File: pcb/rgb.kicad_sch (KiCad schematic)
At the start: 29 parts, among them J1 2.54-2*8P, J3 B4PS-VH, J4 TYPE-C-31-M-12, J5 TF-01A, J7 B4PS-VH, U4 EVQQ2, U5 ESP32-WROOM-32E, U7 CH340C, U8 SPX3819M5-L, U9 CH224K

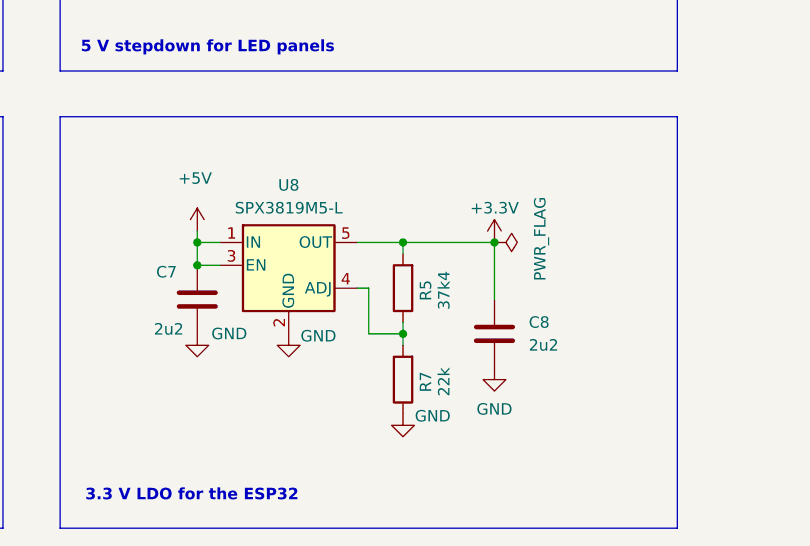
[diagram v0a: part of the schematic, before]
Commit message: pcb: increase esp32 voltage slightly
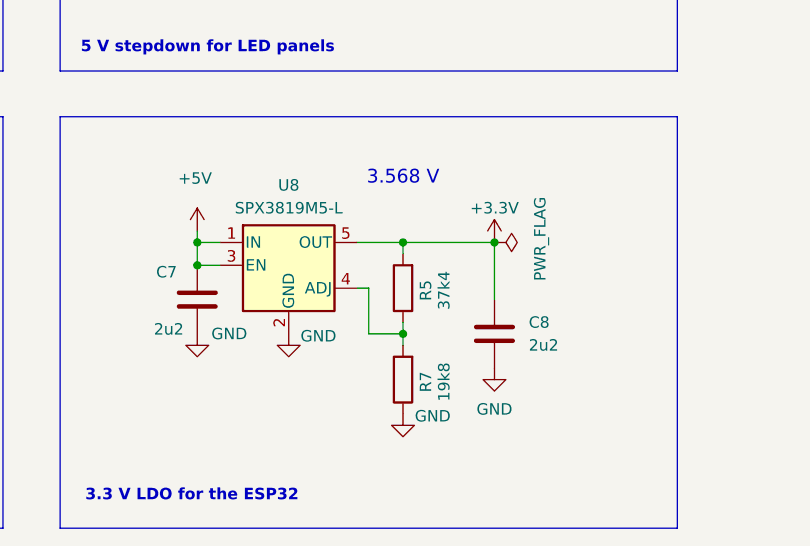
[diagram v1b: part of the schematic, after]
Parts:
- R7: value 22k -> 19k8
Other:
- note added: "3.568 V"
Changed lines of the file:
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@@
+		)
+	)
+	(text "3.568 V"
+		(exclude_from_sim no)
+		(at 133.35 144.018 0)
+		(effects
+			(font
+				(size 1.524 1.524)
+			)
 		)
 	)
@@
 			)
 		)
-		(property "Value" "22k"
+		(property "Value" "19k8"
 			(at 137.922 166.624 90)
 			(effects

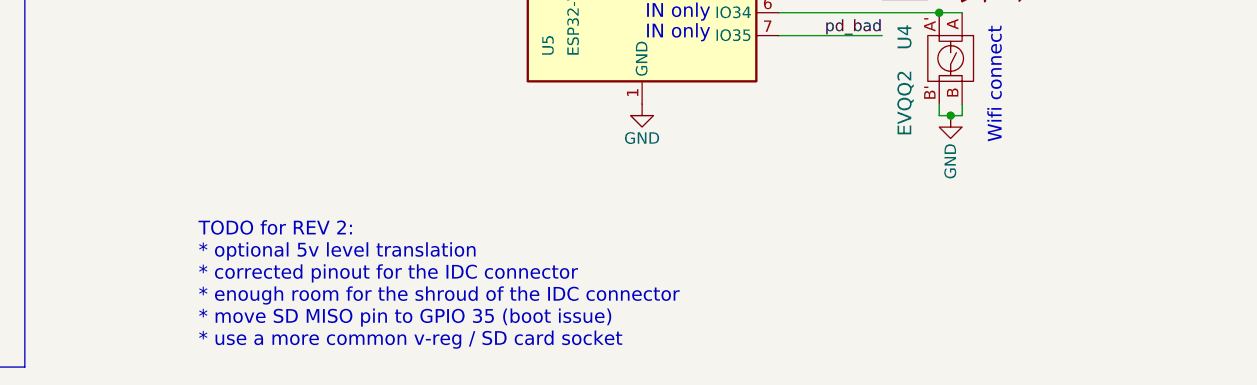
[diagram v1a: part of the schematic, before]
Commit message: hardware bug, swap IO 12 and 33
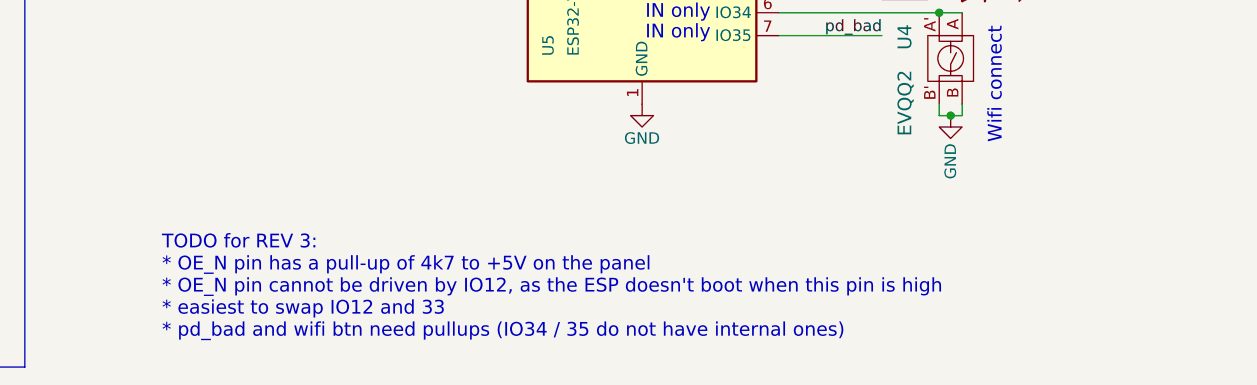
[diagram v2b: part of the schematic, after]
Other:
- note added: "TODO for REV 3: * OE_N pin has a pull-up of 4k7 to +5V on the panel * OE_N pin cannot be driven by IO12, as the ESP doesn't boot when this pin is high * easiest to swap IO12 and 33 * pd_bad and wifi btn need pullups (IO34 / 35 do not have internal ones)"
- note removed: "TODO for REV 2: * optional 5v level translation * corrected pinout for the IDC connector * enough room for the shroud of the IDC connector * move SD MISO pin to GPIO 35 (boot issue) * use a more common v-reg / SD card socket"
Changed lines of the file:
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@@
 		)
 	)
-	(text "TODO for REV 2:\n* optional 5v level translation\n* corrected pinout for the IDC connector\n* enough room for the shroud of the IDC connector\n* move SD MISO pin to GPIO 35 (boot issue)\n* use a more common v-reg / SD card socket"
+	(text "TODO for REV 3:\n* OE_N pin has a pull-up of 4k7 to +5V on the panel\n* OE_N pin cannot be driven by IO12, as the ESP doesn't boot when this pin is high\n* easiest to swap IO12 and 33\n* pd_bad and wifi btn need pullups (IO34 / 35 do not have internal ones)\n"
 		(exclude_from_sim no)
-		(at 183.134 180.848 0)
+		(at 179.07 179.832 0)
 		(effects
 			(font

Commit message: schematic: one more item for the todo list
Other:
- note added: "* Connect SD card to the fixed pins of the MMC-interface. Because the SD-SPI driver in IDF-V5 does seek very slowly"
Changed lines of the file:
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@@
+		)
+	)
+	(text "*  Connect SD card to the fixed pins of the MMC-interface.\n   Because the SD-SPI driver in IDF-V5 does seek very slowly"
+		(exclude_from_sim no)
+		(at 198.12 186.69 0)
+		(effects
+			(font
+				(size 1.524 1.524)
+			)
+			(justify left bottom)
 		)
 	)

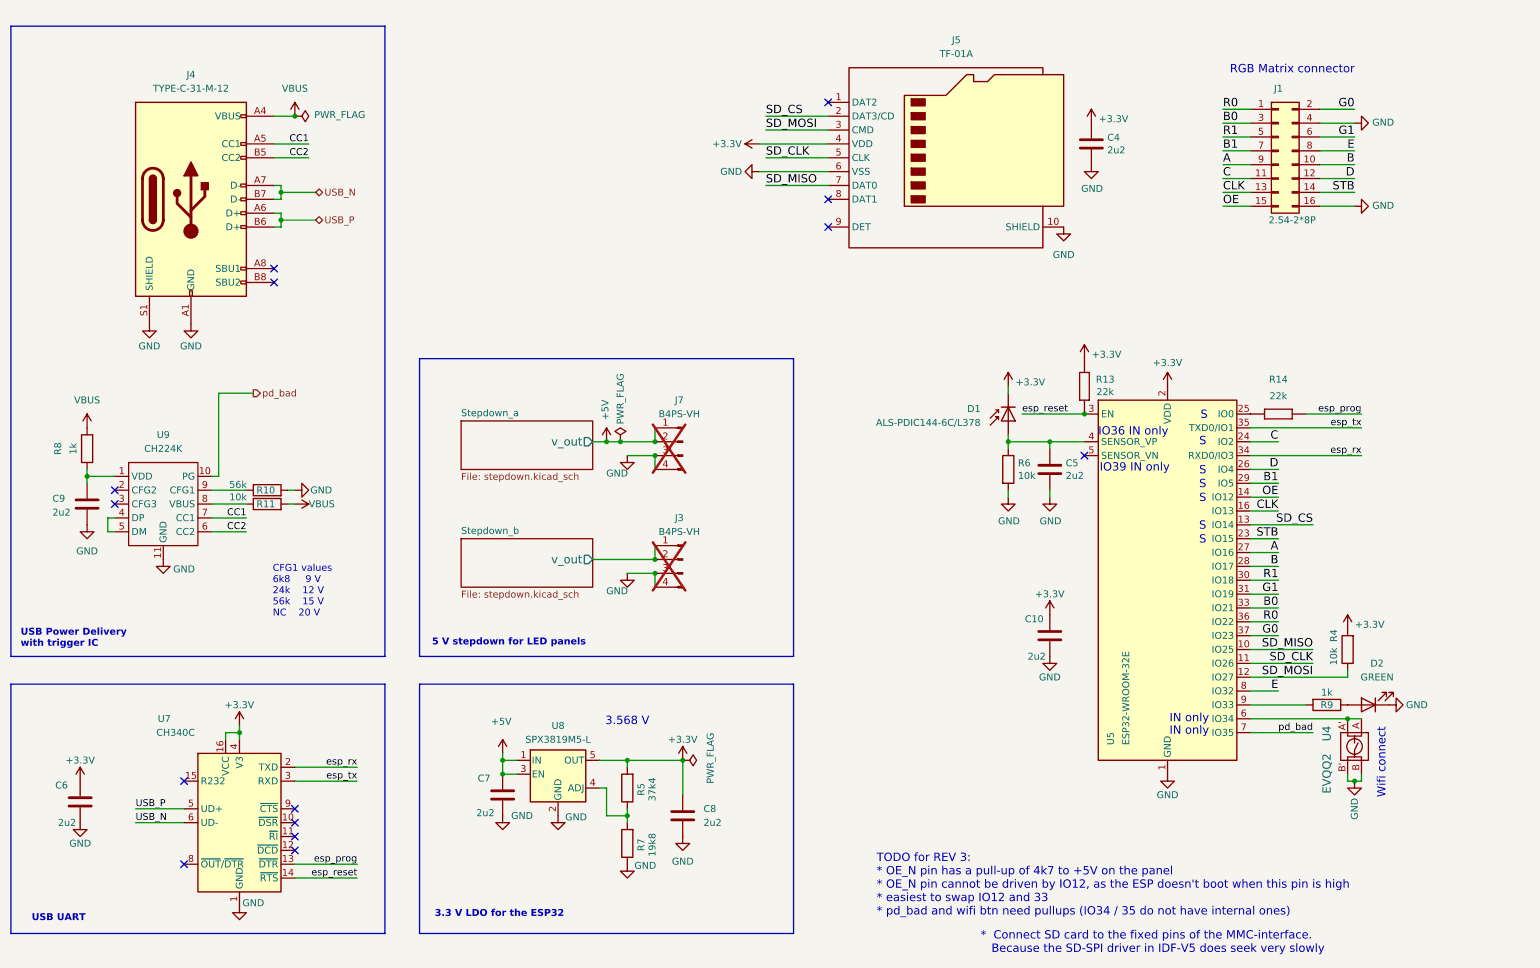
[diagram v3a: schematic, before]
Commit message: first sketch of optimized pinout
Support SD MMC mode x4
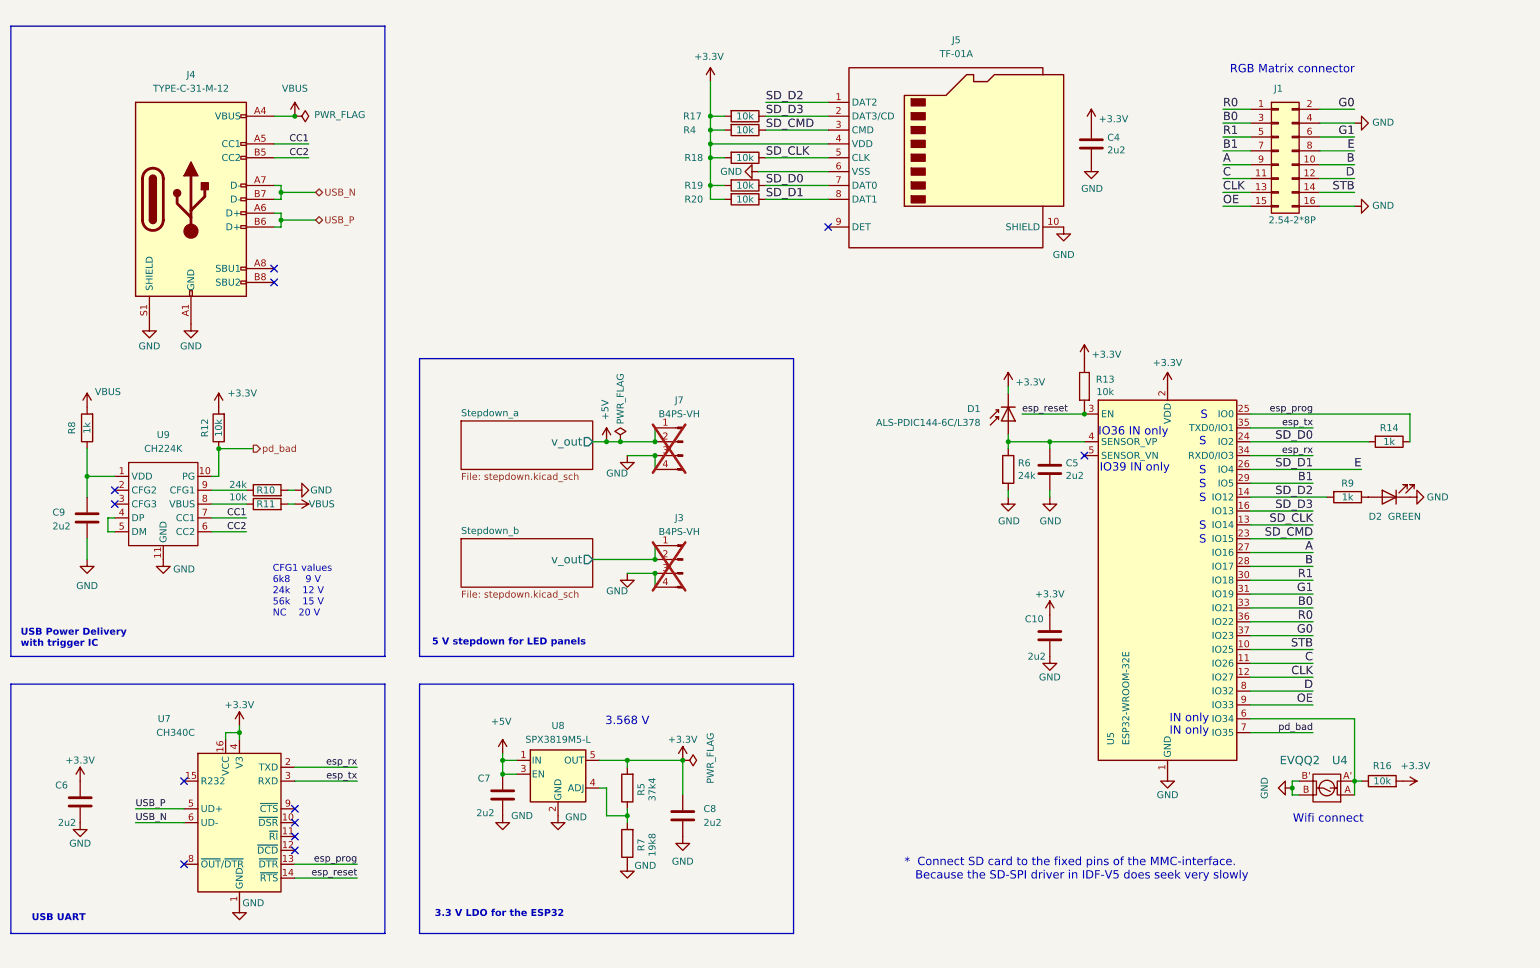
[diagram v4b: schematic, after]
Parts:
- removed R14: 22k, Resistor_SMD:R_0603_1608Metric, symbol passive_resistors:R_0603_1%
- added R12, R16, R17, R18, R19, R20: 10k, Resistor_SMD:R_0603_1608Metric, symbol Device:R
- added R14: 1k, Resistor_SMD:R_0603_1608Metric, symbol Device:R
- R10: value 56k -> 24k
- R13: value 22k -> 10k
- R6: value 10k -> 24k
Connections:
- net +3.3V: now also R12.2, R16.2, R17.2, R18.2, R19.2, R20.2
- net C: now also U5.11 (IO26); no longer U5.24 (IO2)
- net CLK: now also U5.12 (IO27); no longer U5.16 (IO13)
- net D: now also U5.8 (IO32); no longer U5.26 (IO4)
- net E: now also J5.8 (DAT1), U5.26 (IO4), R20.1; no longer U5.8 (IO32)
- net OE: now also U5.9 (IO33); no longer U5.14 (IO12)
- net SD_CLK: now also U5.13 (IO14), R18.1; no longer U5.11 (IO26)
- net STB: now also U5.10 (IO25); no longer U5.23 (IO15)
- net esp_prog: now also U5.25 (IO0), R14.1
- net pd_bad: now also R12.1
- net at U4.A, U4.A', U5.6 (IO34): now also R16.1
- net SD_D2: now reaches R9.2
- net SD_D2: now also J5.1 (DAT2), U5.14 (IO12); no longer U5.9 (IO33)
- net SD_CS renamed SD_D3
- net SD_D3: now also U5.16 (IO13), R17.1; no longer U5.13 (IO14)
- net SD_MISO renamed SD_D0
- net SD_D0: now also U5.24 (IO2), R14.2, R19.1; no longer U5.10 (IO25)
- net SD_MOSI renamed SD_CMD
- net SD_CMD: now also U5.23 (IO15); no longer U5.12 (IO27)
- no-connect marks 14 -> 12
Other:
- note removed: "TODO for REV 3: * OE_N pin has a pull-up of 4k7 to +5V on the panel * OE_N pin cannot be driven by IO12, as the ESP doesn't boot when this pin is high * easiest to swap IO12 and 33 * pd_bad and wifi btn need pullups (IO34 / 35 do not have internal ones)"
- moved on the sheet: C9, D2, R8, R9, U4

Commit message: finalize pinout
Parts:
- added SW1: MS-22C01-G010, symbol Switch:SW_Slide_DPDT
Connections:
- net SD_D3 is gone; now on net E: J5.2 (DAT3/CD), R17.1, U5.16 (IO13)
- net E: no longer J5.8 (DAT1), R20.1, U5.26 (IO4)
- net USB_N: now also SW1.2 (B); no longer U7.6 (UD-)
- net USB_P: now also SW1.5 (B); no longer U7.5 (UD+)
- net USB_N_P: now reaches U9.5 (DM)
- net USB_N_P: now also SW1.3 (C); no longer U9.4 (DP)
- new net SD_D1: J5.8 (DAT1), R20.1, U5.26 (IO4)
- new net USB_N_S: SW1.1 (A), U7.6 (UD-)
- new net USB_P_P: SW1.4 (A), U9.4 (DP)
- new net USB_P_S: SW1.6 (C), U7.5 (UD+)
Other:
- note added: "Either / Or: 4 wire SD LED + ADDR E"
- note added: "QC quick charge"
- note added: "UART"
- note added: "USB mode selection To enable UART for PC communiation, switch to UART To get > 5 V from a USB type-A cable, switch to QC"
- note removed: "* Connect SD card to the fixed pins of the MMC-interface. Because the SD-SPI driver in IDF-V5 does seek very slowly"
- moved on the sheet: C9, D2, J4, R9

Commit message: add note about GPIO12 to schematic
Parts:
- added R21: 10k, Resistor_SMD:R_0603_1608Metric, symbol Device:R
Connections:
- net SD_D2: now also R21.1
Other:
- note added: "Before SD_D2 pullup is populated, 3.3 V flash efuse must be burned"
- note added: "Choose: either 4 wire SD or LED + ADDR E"
- note added: "Untested features: * USB QC support (for > 5 V over type A cables) * SD-MMC with 4 data-lines"
- note removed: "Either / Or: 4 wire SD LED + ADDR E"
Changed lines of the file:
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@@
 		)
 	)
-	(text "Either / Or:\n4 wire SD\nLED + ADDR E"
+	(text "Choose:\neither 4 wire SD\nor LED + ADDR E"
 		(exclude_from_sim no)
 		(at 272.542 111.76 0)
@@
 		)
 	)
+	(text "Before SD_D2 pullup is populated,\n3.3 V flash efuse must be burned"
+		(exclude_from_sim no)
+		(at 163.068 16.764 0)
+		(effects
+			(font
+				(size 1.524 1.524)
+			)
+			(href "https://docs.espressif.com/projects/esp-idf/en/stable/esp32/api-reference/peripherals/sd_pullup_requirements.html#conflicts-between-bootstrap-and-sdio-on-dat2")
+		)
+	)
 	(text "S"
 		(exclude_from_sim no)
@@
 		)
 	)
+	(text "Untested features:\n  * USB QC support (for > 5 V over type A cables)\n  * SD-MMC with 4 data-lines"
+		(exclude_from_sim no)
+		(at 180.594 172.72 0)
+		(effects
+			(font
+				(size 1.524 1.524)
+			)
+			(justify left)
+		)
+	)
 	(text "S"
 		(exclude_from_sim no)
@@
 					(unit 1)
 				)
+			)
+		)
+	)
+	(symbol
+		(lib_id "Device:R")
+		(at 154.94 30.48 270)
+		(unit 1)
+		(exclude_from_sim no)
+		(in_bom yes)
+		(on_board yes)
+		(dnp yes)
+		(property "Reference" "R21"
+			(at 145.288 30.48 90)
+			(effects
+				(font
+					(size 1.27 1.27)
+				)
+			)
+		)
+		(property "Value" "10k"
+			(at 154.94 30.48 90)
+			(effects
+				(font
+					(size 1.27 1.27)
+				)
+			)
+		)
+		(property "Footprint" "Resistor_SMD:R_0603_1608Metric"
+			(at 154.94 28.702 90)
+			(effects
+				(font
+					(size 1.27 1.27)
+				)
+				(hide yes)
+			)
+		)
+		(property "Datasheet" ""
+			(at 154.94 30.48 0)
+			(effects
+				(font
+					(size 1.27 1.27)
+				)
+				(hide yes)
+			)
+		)
+		(property "Description" ""
+			(at 154.94 30.48 0)
+			(effects
+				(font
+					(size 1.27 1.27)
+				)
+				(hide yes)
+			)
+		)
+		(pin "1"
+		)
+		(pin "2"
+		)
+		(instances
+			(project "rgb"
+				(path "/e2cadc20-e108-4c6f-b279-00d9d28fa9da"
+					(reference "R21")
+					(unit 1)
+				)

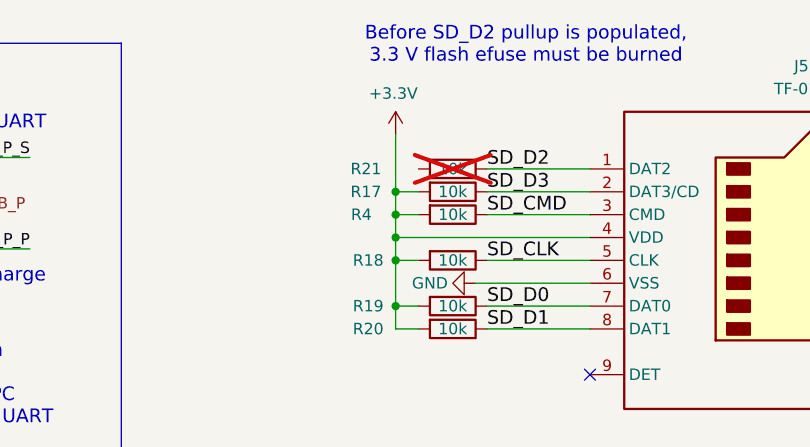
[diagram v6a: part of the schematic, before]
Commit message: schematic: add a missing wire
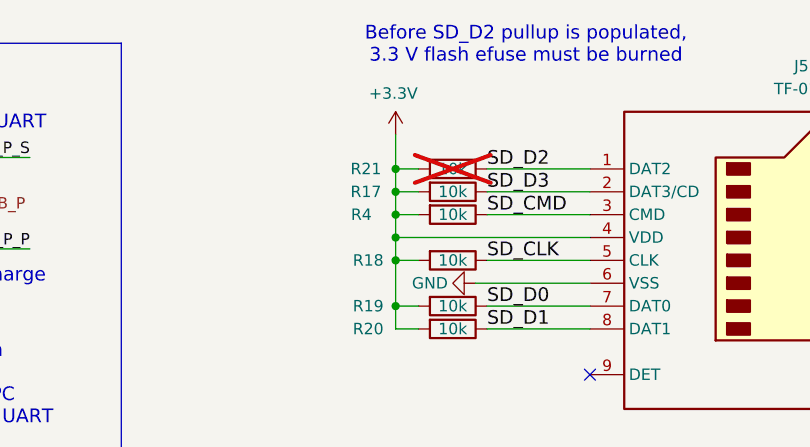
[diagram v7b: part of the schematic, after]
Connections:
- net +3.3V: now also R21.2
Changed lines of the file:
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@@
+	)
+	(junction
+		(at 148.59 30.48)
+		(diameter 0)
+		(color 0 0 0 0)
 	)
 	(junction
@@
 	(wire
 		(pts
-			(xy 148.59 26.67) (xy 148.59 33.02)
+			(xy 148.59 26.67) (xy 148.59 30.48)
 		)
 		(stroke
@@
 	(wire
 		(pts
+			(xy 148.59 30.48) (xy 151.13 30.48)
+		)
+		(stroke
+			(width 0)
+			(type default)
+		)
+	)
+	(wire
+		(pts
 			(xy 110.49 153.67) (xy 113.03 153.67)
 		)
@@
 		)
 		(stroke
+			(width 0)
+			(type default)
+		)
+	)
+	(wire
+		(pts
+			(xy 148.59 30.48) (xy 148.59 33.02)
+		)
+		(stroke
